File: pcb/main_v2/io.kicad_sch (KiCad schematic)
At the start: 0 parts

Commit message: updarted schematic and simulation
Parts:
- added J701: Conn_01x03_Pin, Connector_PinHeader_2.54mm:PinHeader_1x03_P2.54mm_Vertical, symbol Connector:Conn_01x03_Pin
- added J702: Conn_02x10_Odd_Even, symbol Connector_Generic:Conn_02x10_Odd_Even
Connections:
- new net +3.3V: J702.10 (Pin_10), J702.14 (Pin_14), J702.2 (Pin_2), J702.20 (Pin_20), J702.4 (Pin_4)
- new net +5V: J702.18 (Pin_18)
- new net GND: J702.17 (Pin_17), J702.19 (Pin_19)
- new net PA DET Output: J702.11 (Pin_11)
- new net PA Enable: J702.9 (Pin_9)
- new net PLL: Chip Enable: J702.1 (Pin_1)
- new net PLL: Lock Detect: J702.7 (Pin_7)
- new net PLL: MUXOUT: J702.5 (Pin_5)
- new net PLL: Power Down: J702.3 (Pin_3)
- new net Power Enable: J702.13 (Pin_13)
- new net Power Faulty: J702.15 (Pin_15)
- new net SPI: CLK: J701.1 (Pin_1)
- new net SPI: DATA: J701.2 (Pin_2)
- new net SPI: Load Enable: J701.3 (Pin_3)
- no-connect marks 0 -> 4
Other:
- note added: "SPI"
- note added: "high: 1.8 bis 3.6 v I = 300 uA"
- note added: "todo: ADC für vdet hinzufügen. RFSoc hat nur analog io"
- note added: "todo: check pullup/down"
- note added: "todo: treiber für enable signal"
- note added: "todo: treiber für spi notwendig?"

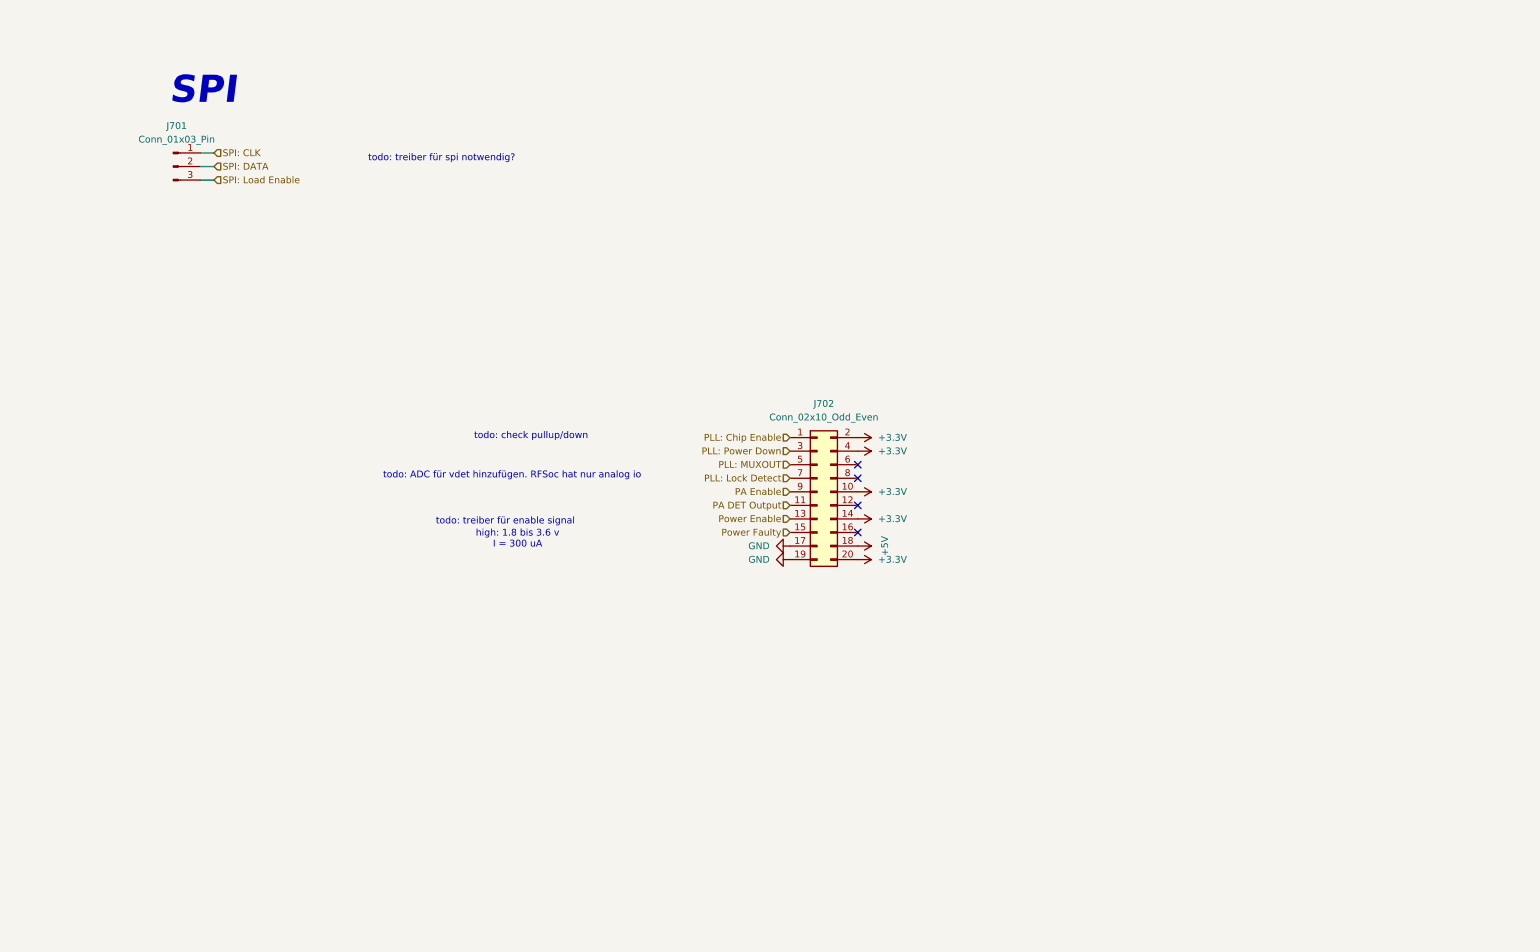
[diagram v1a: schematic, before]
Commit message: added noise calc for simulation
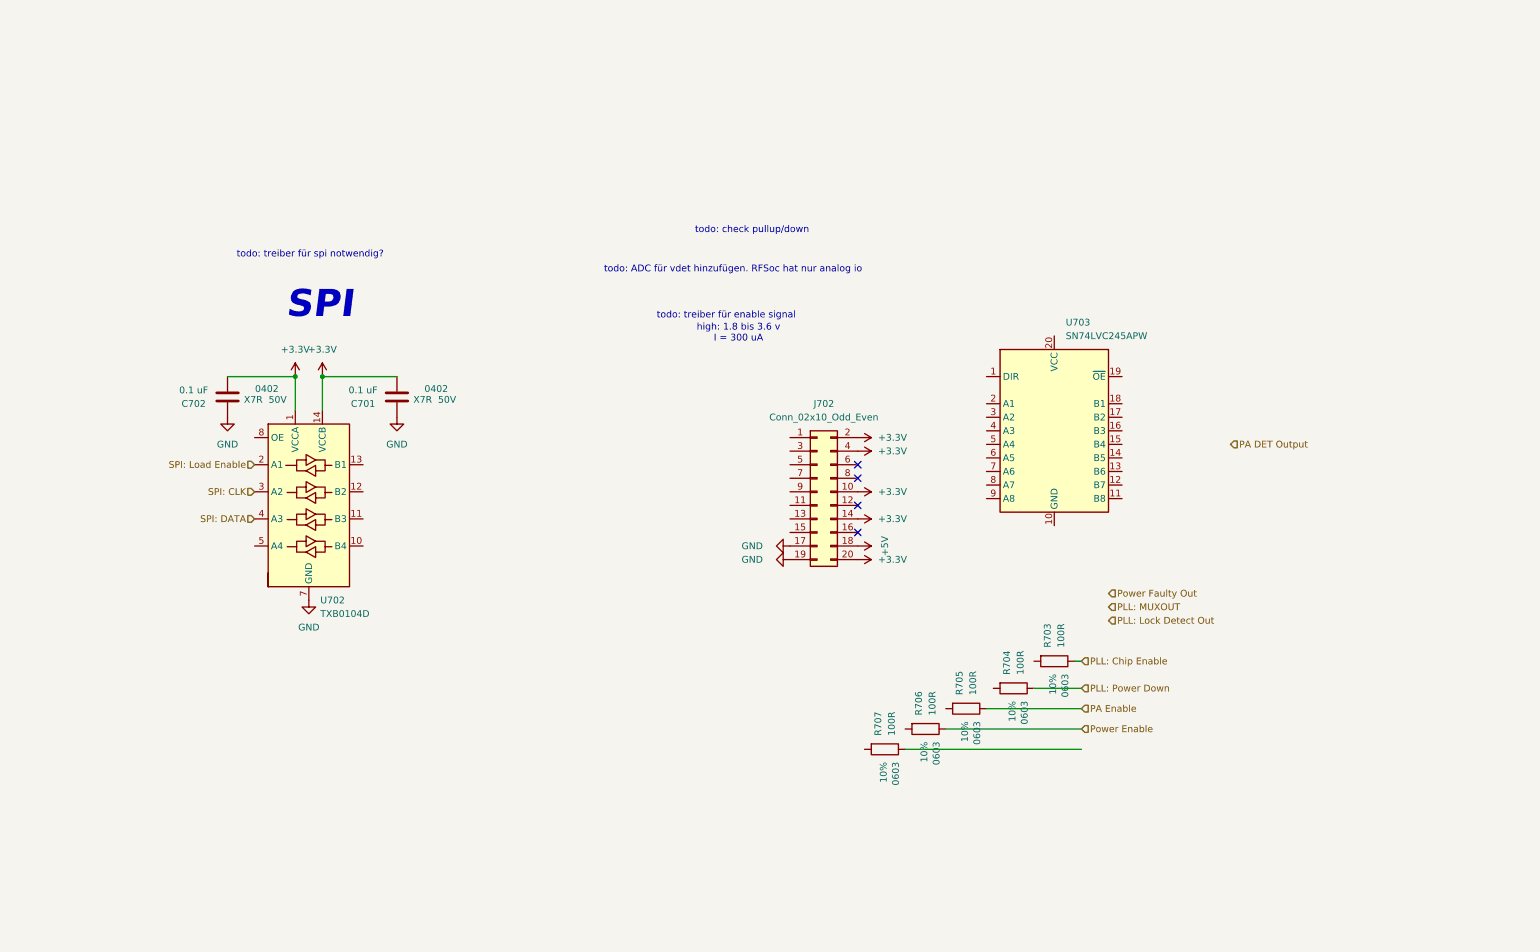
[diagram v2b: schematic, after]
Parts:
- removed J701: Conn_01x03_Pin, Connector_PinHeader_2.54mm:PinHeader_1x03_P2.54mm_Vertical, symbol Connector:Conn_01x03_Pin
- added C701, C702: 0.1 uF, Capacitor_SMD:C_0402_1005Metric, symbol Device:C
- added R703, R704, R705, R706, R707: 100R, Resistor_SMD:R_0603_1608Metric, symbol Device:R
- added U702: TXB0104D, Package_SO:SOIC-14_3.9x8.7mm_P1.27mm, symbol Logic_LevelTranslator:TXB0104D
- added U703: SN74LVC245APW, Package_SO:TSSOP-20_4.4x6.5mm_P0.65mm, symbol Logic_LevelTranslator:SN74LVC245APW
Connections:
- net +3.3V: now also C701.1, C702.1, U702.1 (VCCA), U702.14 (VCCB)
- net GND: now also C701.2, C702.2, U702.7 (GND)
- net PA DET Output: no longer J702.11 (Pin_11)
- net PA Enable: now also R705.1; no longer J702.9 (Pin_9)
- net PLL: Chip Enable: now also R703.1; no longer J702.1 (Pin_1)
- net PLL: MUXOUT: no longer J702.5 (Pin_5)
- net PLL: Power Down: now also R704.1; no longer J702.3 (Pin_3)
- net Power Enable: now also R706.1; no longer J702.13 (Pin_13)
- net SPI: CLK: now also U702.3 (A2)
- net SPI: DATA: now also U702.4 (A3)
- net SPI: Load Enable: now also U702.2 (A1)
- net PLL: Lock Detect: no longer names the net of J702.7 (Pin_7)
- net Power Faulty: no longer names the net of J702.15 (Pin_15)

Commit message: updated io schematic
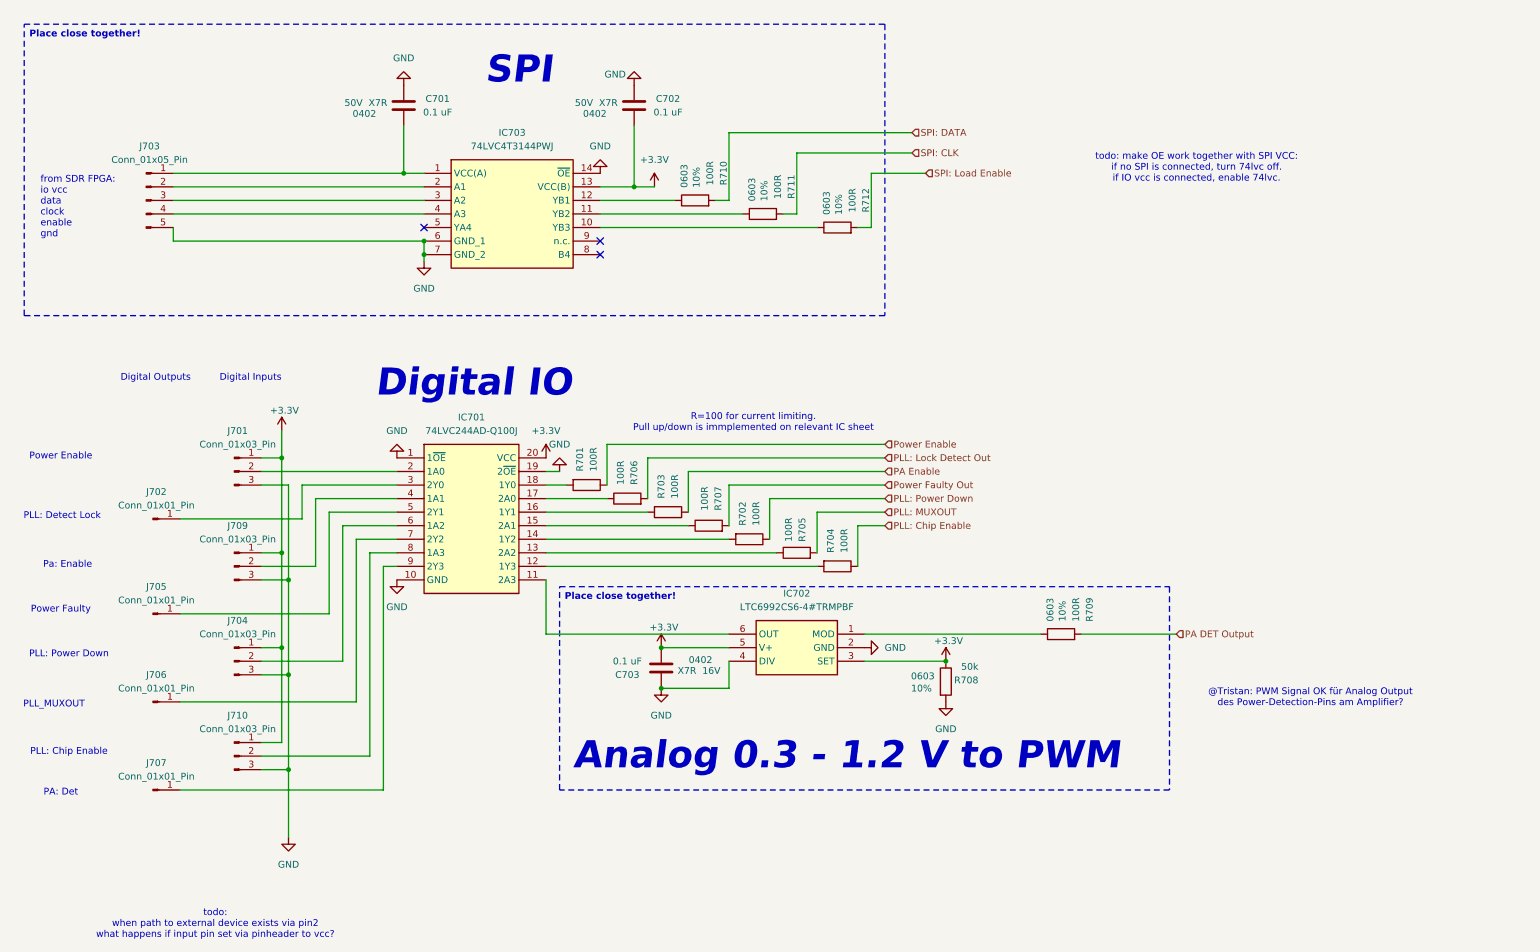
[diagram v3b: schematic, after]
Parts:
- removed J702: Conn_02x10_Odd_Even, symbol Connector_Generic:Conn_02x10_Odd_Even
- removed U702: TXB0104D, Package_SO:SOIC-14_3.9x8.7mm_P1.27mm, symbol Logic_LevelTranslator:TXB0104D
- removed U703: SN74LVC245APW, Package_SO:TSSOP-20_4.4x6.5mm_P0.65mm, symbol Logic_LevelTranslator:SN74LVC245APW
- added C703: 0.1 uF, Capacitor_SMD:C_0402_1005Metric, symbol Device:C
- added IC701: 74LVC244AD-Q100J, My Footprints:SOIC127P1032X265-20N, symbol My Symbols:74LVC244AD-Q100J
- added IC702: LTC6992CS6-4#TRMPBF, My Footprints:SOT95P280X100-6N, symbol My Symbols:LTC6992CS6-4#TRMPBF
- added IC703: 74LVC4T3144PWJ, SOP65P640X110-14N, symbol My Symbols:74LVC4T3144PWJ
- added J701, J704, J709, J710: Conn_01x03_Pin, Connector_PinHeader_2.54mm:PinHeader_1x03_P2.54mm_Vertical, symbol Connector:Conn_01x03_Pin
- added J702, J705, J706, J707: Conn_01x01_Pin, Connector_PinHeader_2.54mm:PinHeader_1x01_P2.54mm_Vertical, symbol Connector:Conn_01x01_Pin
- added J703: Conn_01x05_Pin, Connector_PinHeader_2.54mm:PinHeader_1x05_P2.54mm_Vertical, symbol Connector:Conn_01x05_Pin
- added R701, R702, R709, R710, R711, R712: 100R, Resistor_SMD:R_0603_1608Metric, symbol Device:R
- added R708: 50k, Resistor_SMD:R_0603_1608Metric, symbol Device:R
- R703, R704, R705, R706, R707: Package 0603 -> (none); Tolerance 10% -> (none)
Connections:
- net +3.3V: now also C703.1, IC701.20 (VCC), IC702.3 (SET), IC702.5 (V+), IC703.13 (VCC(B)), J701.1 (Pin_1), J704.1 (Pin_1), J709.1 (Pin_1), J710.1 (Pin_1), R708.1; no longer C701.1
- net GND: now also C703.2, IC701.1 (1~{OE}), IC701.10 (GND), IC701.19 (2~{OE}), IC702.2 (GND), IC702.4 (DIV), IC703.14 (~{OE}), IC703.6 (GND_1), IC703.7 (GND_2), J701.3 (Pin_3), J703.5 (Pin_5), J704.3 (Pin_3), J709.3 (Pin_3), J710.3 (Pin_3), R708.2
- net PA DET Output: now also R709.2
- net PA Enable: now also R703.1; no longer R705.1
- net PLL: Chip Enable: now also R704.1; no longer R703.1
- net PLL: Lock Detect Out: now also R706.2
- net PLL: MUXOUT: now also R705.2
- net PLL: Power Down: now also R702.1; no longer R704.1
- net Power Enable: now also R701.1; no longer R706.1
- net Power Faulty Out: now also R707.2
- net SPI: CLK: now also R711.2
- net SPI: DATA: now also R710.2
- net SPI: Load Enable: now also R712.2
- net at R704.2: now also IC701.12 (1Y3)
- net at R707.1: now also IC701.15 (2A1)
- net at R703.2: now also IC701.16 (1Y1)
- new net: IC701.6 (1A2), J704.2 (Pin_2)
- new net: IC703.12 (YB1), R710.1
- new net: IC701.7 (2Y2), J706.1 (Pin_1)
- new net: C701.1, IC703.1 (VCC(A)), J703.1 (Pin_1)
- new net: IC703.2 (A1), J703.2 (Pin_2)
- new net: IC703.3 (A2), J703.3 (Pin_3)
- new net: IC703.4 (A3), J703.4 (Pin_4)
- new net: IC703.10 (YB3), R712.1
- new net: IC701.11 (2A3), IC702.6 (OUT)
- new net: IC701.13 (2A2), R705.1
- new net: IC701.14 (1Y2), R702.2
- new net: IC701.17 (2A0), R706.1
- new net: IC701.18 (1Y0), R701.2
- new net: IC701.2 (1A0), J701.2 (Pin_2)
- new net: IC701.3 (2Y0), J702.1 (Pin_1)
- new net: IC701.4 (1A1), J709.2 (Pin_2)
- new net: IC701.5 (2Y1), J705.1 (Pin_1)
- new net: IC701.8 (1A3), J710.2 (Pin_2)
- new net: IC701.9 (2Y3), J707.1 (Pin_1)
- new net: IC703.11 (YB2), R711.1
- new net: IC702.1 (MOD), R709.1
- no-connect marks 4 -> 3
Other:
- note added: "@Tristan: PWM Signal OK für Analog Output des Power-Detection-Pins am Amplifier?"
- note added: "Analog 0.3 - 1.2 V to PWM"
- note added: "Digital IO"
- note added: "Digital Inputs"
- note added: "Digital Outputs"
- note added: "PA: Det"
- note added: "PLL: Chip Enable"
- note added: "PLL: Detect Lock"
- note added: "PLL: Power Down"
- note added: "PLL_MUXOUT"
- note added: "Pa: Enable"
- note added: "Power Enable"
- note added: "Power Faulty"
- note added: "R=100 for current limiting. Pull up/down is immplemented on relevant IC sheet"
- note added: "from SDR FPGA: io vcc data clock enable gnd"
- note added: "todo: make OE work together with SPI VCC: if no SPI is connected, turn 74lvc off. if IO vcc is connected, enable 74lvc."
- note added: "todo: when path to external device exists via pin2 what happens if input pin set via pinheader to vcc?"
- note removed: "high: 1.8 bis 3.6 v I = 300 uA"
- note removed: "todo: ADC für vdet hinzufügen. RFSoc hat nur analog io"
- note removed: "todo: check pullup/down"
- note removed: "todo: treiber für enable signal"
- note removed: "todo: treiber für spi notwendig?"

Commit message: update bom
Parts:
- added R713: 50k, Resistor_SMD:R_0603_1608Metric, symbol Device:R
- IC701: renamed from IC703; footprint SOP65P640X110-14N -> My Footprints:SOP65P640X110-14N
- renumbered IC701 to IC702, IC702 to IC703, J703 to J701, J701 to J702, J702 to J703, J709 to J704, J704 to J706, J706 to J707, J710 to J708, J707 to J709, R710 to R701, R711 to R702, R712 to R703, R701 to R704, R706 to R705, R703 to R706, R702 to R708, R705 to R709, R704 to R710, R709 to R711, R708 to R712
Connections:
- net +3.3V: now also R713.1
- net GND: now also R713.2
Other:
- moved on the sheet: C701, C702, IC701, J701, R701, R702, R703
